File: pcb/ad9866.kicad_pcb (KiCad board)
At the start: 4 copper layers, 48.8 x 41.8 mm, 60 parts, among them CN1 MEC6-140_CONNECTOR_BEMICRO, P1 CONN_2, P10 CONN_1, P13 CONN_1, P14 CONN_1, P15 Si510 73.728, P19 CONN_1, P20 CONN_1, P22 CONN_1, P23 CONN_2, P24 CONN_2, P25 CONN_2, P6 CONN_1, P8 CONN_1, P9 CONN_1, T1 TRANSF_ADT8, T2 TRANSF_ADT2, T3 TRANSF_ADT2, U1 AD9866BCPZ, U2 NCP1117ST33T3G, U3 NCP1117ST33T3G

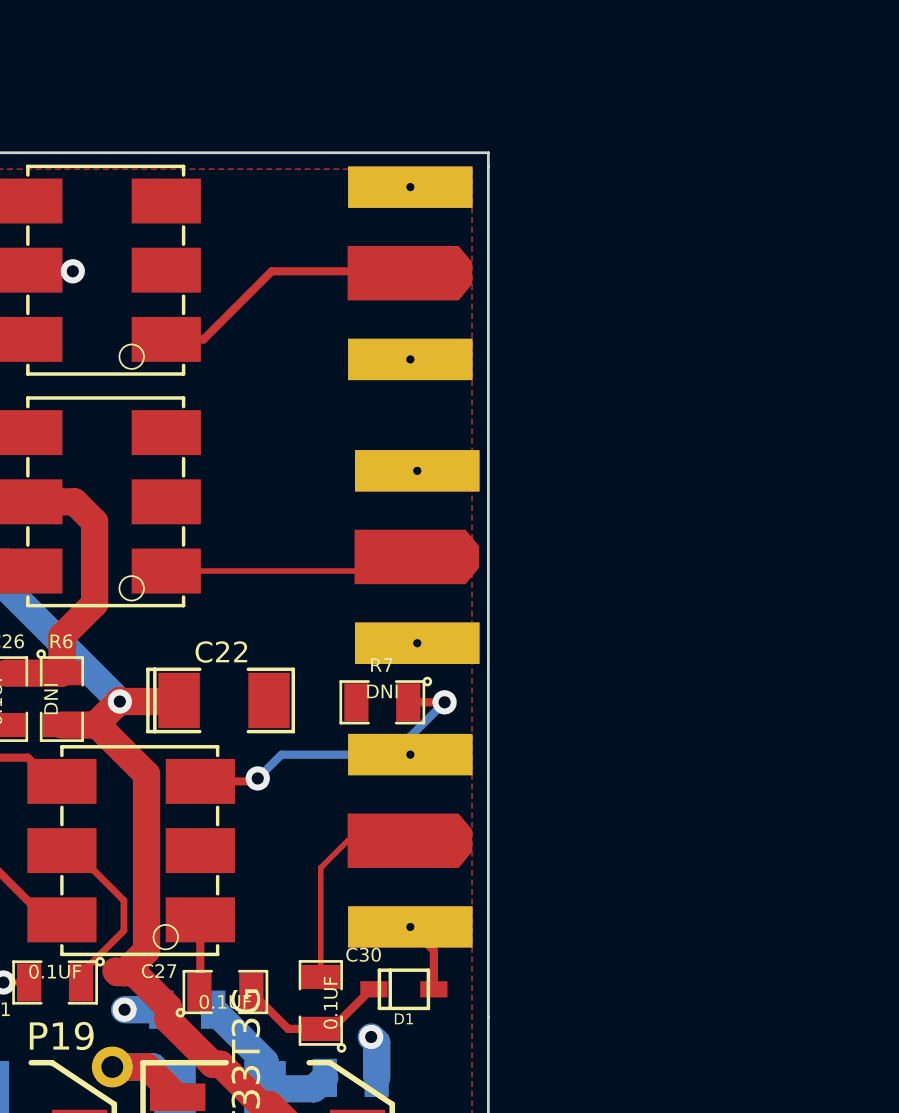
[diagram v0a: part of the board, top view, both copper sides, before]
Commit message: Fixed SMA connectors correctly this time.
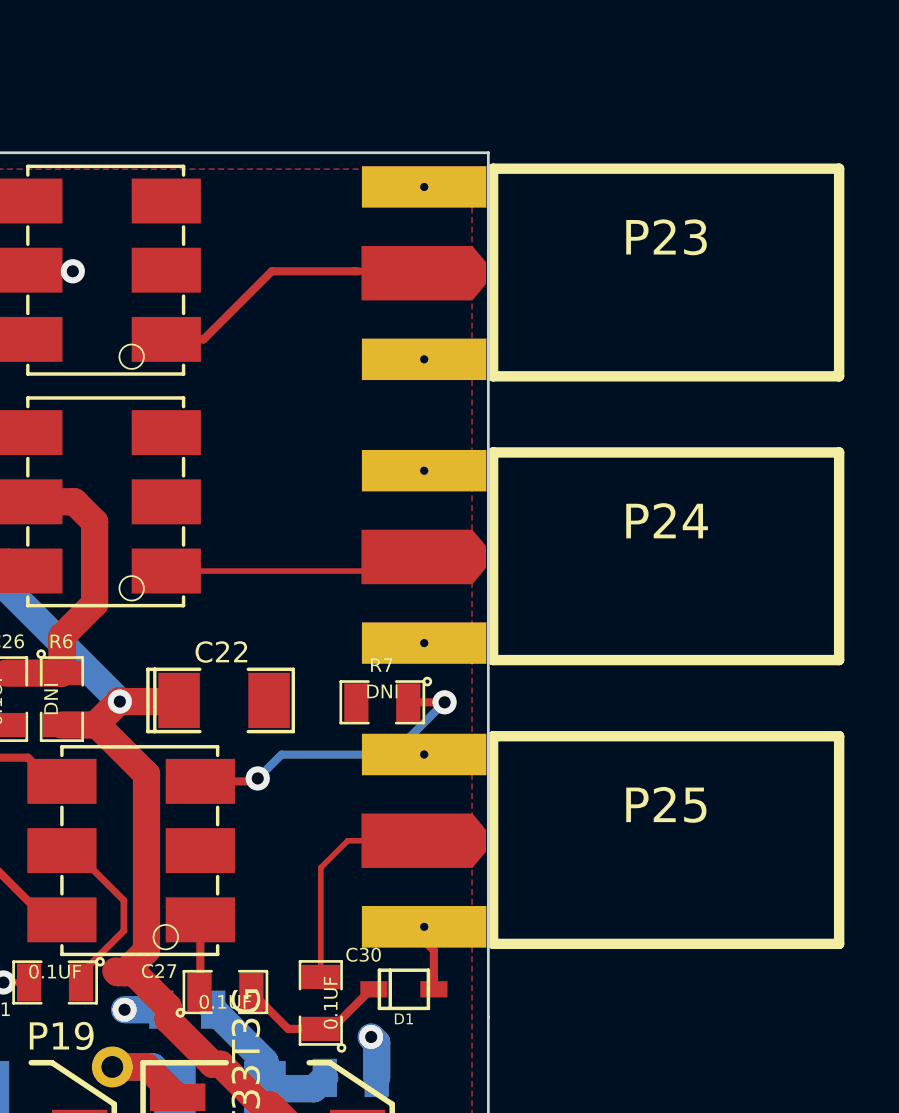
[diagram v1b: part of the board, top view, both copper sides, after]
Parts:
- P23, P24, P25: moved to F.Cu
- moved P23 2.59 mm to (156.0, 86.6)
- moved P25 2.59 mm to (156.0, 107.4)
- moved P24 2.55 mm to (156.0, 97.0)
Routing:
- net Net-(P23-Pad1): track 11.9 -> 17.5 mm
- net Net-(P24-Pad1): track 11.4 -> 13.7 mm
- net Net-(C30-Pad2): track 9.73 -> 12.0 mm

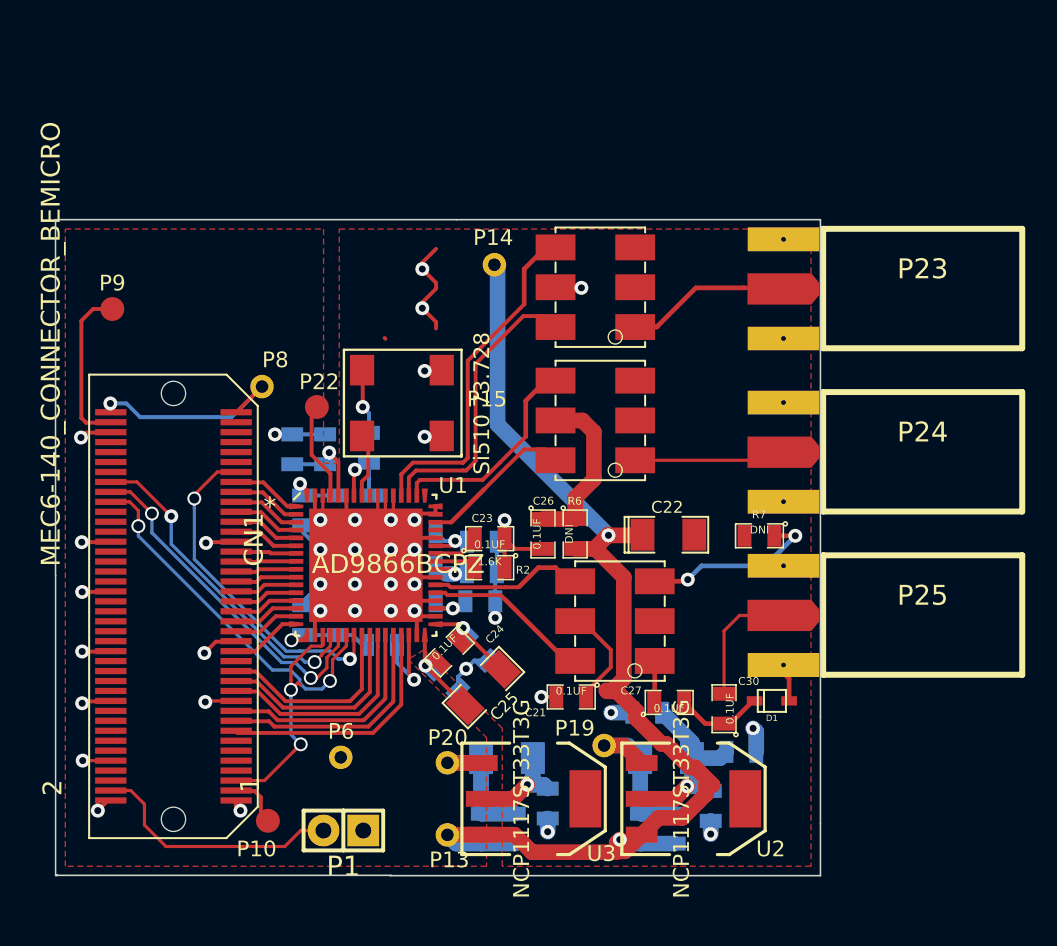
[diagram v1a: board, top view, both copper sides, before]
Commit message: Added the bottom ground plane in.
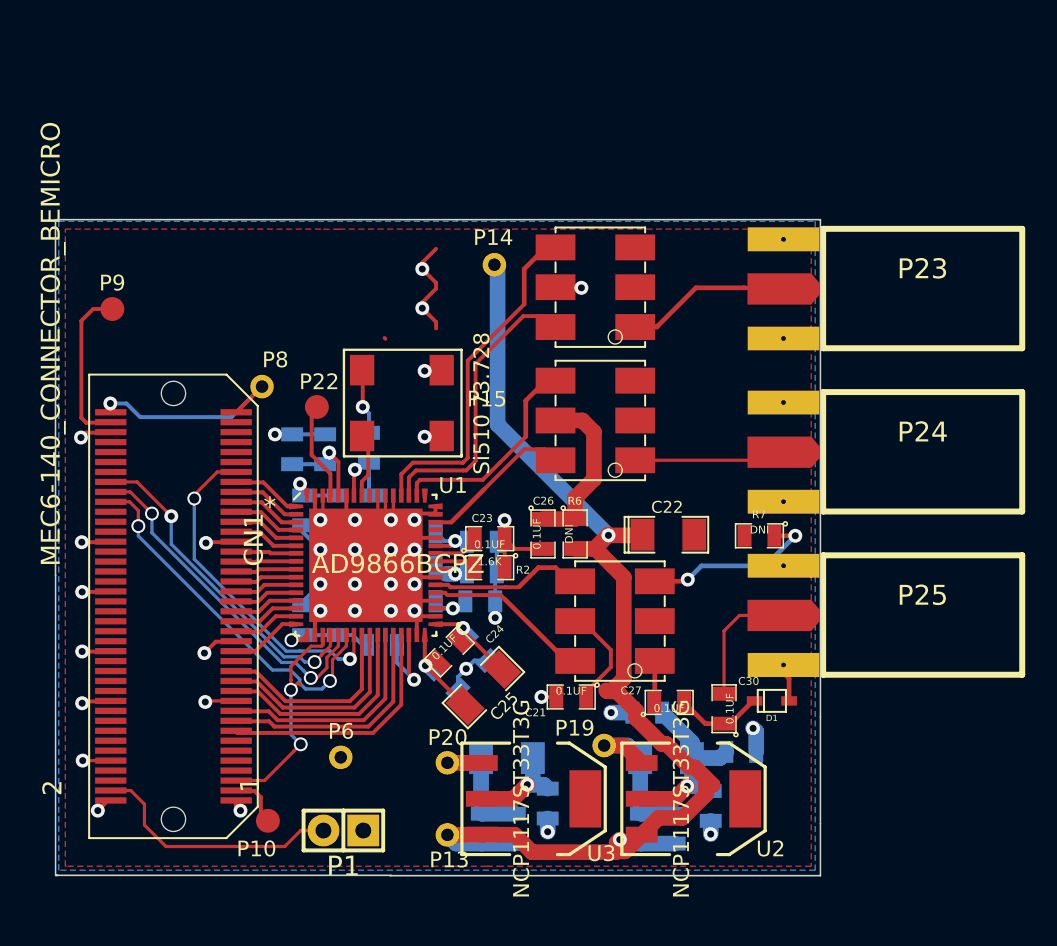
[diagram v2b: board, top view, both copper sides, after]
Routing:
- added copper zone on B.Cu, net GND
